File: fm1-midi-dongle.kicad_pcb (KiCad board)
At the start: 4 copper layers, 18.9 x 26 mm, 30 parts, among them J1 TYPE-C 24P-GTJB 040, J2 TYPE-C-31-M-12, J3 PJ-320D, J4 PJ-320D, U1 CH32X035G8U6, U2 XC6206P332MR, U3 SY6280AAC, U4 H11L1SM

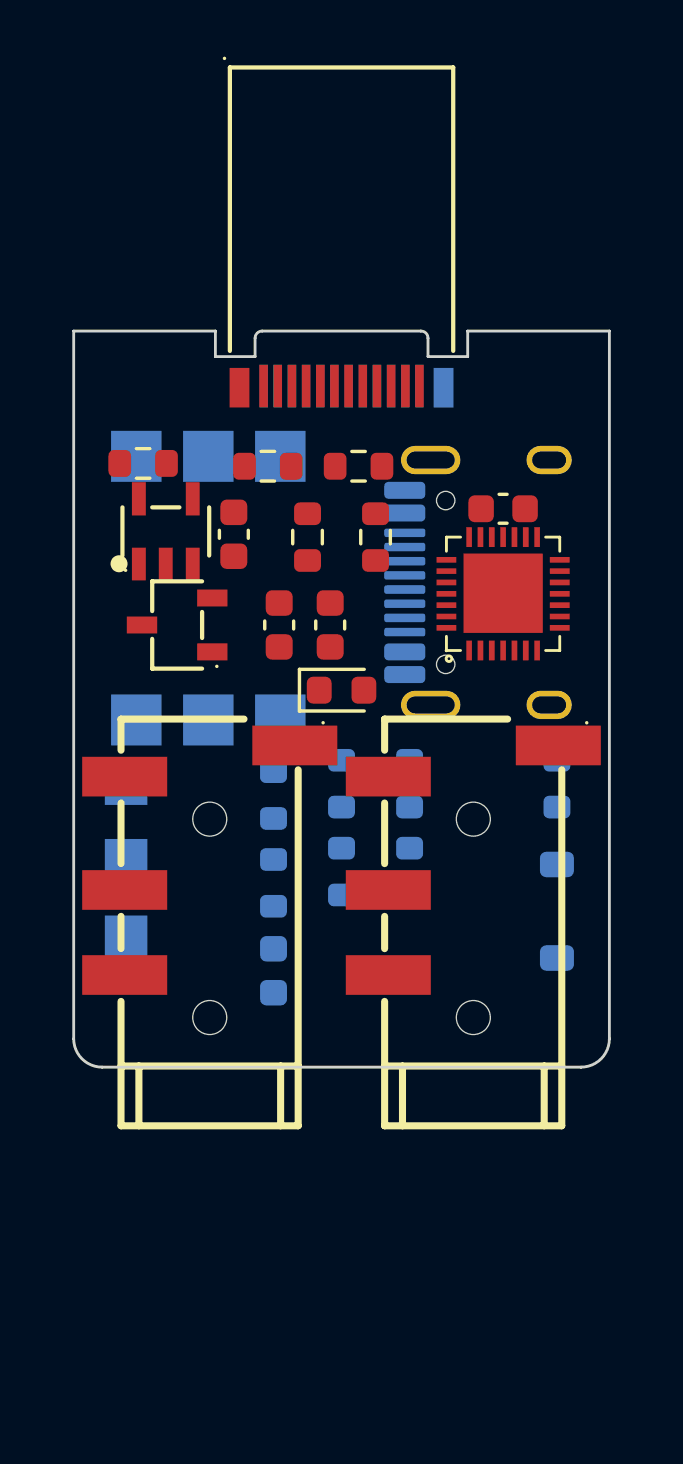
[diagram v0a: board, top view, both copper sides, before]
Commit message: Floorplan v2: signal-priority placement (USB pair straight under the plug, VBUS switch on the back-face pads, MIDI TX on top), 10 mm jack pitch, two inner GND planes, numeric pad-spacing and hole checks
Co-Authored-By: Claude Fable 5.1 <noreply@anthropic.com>
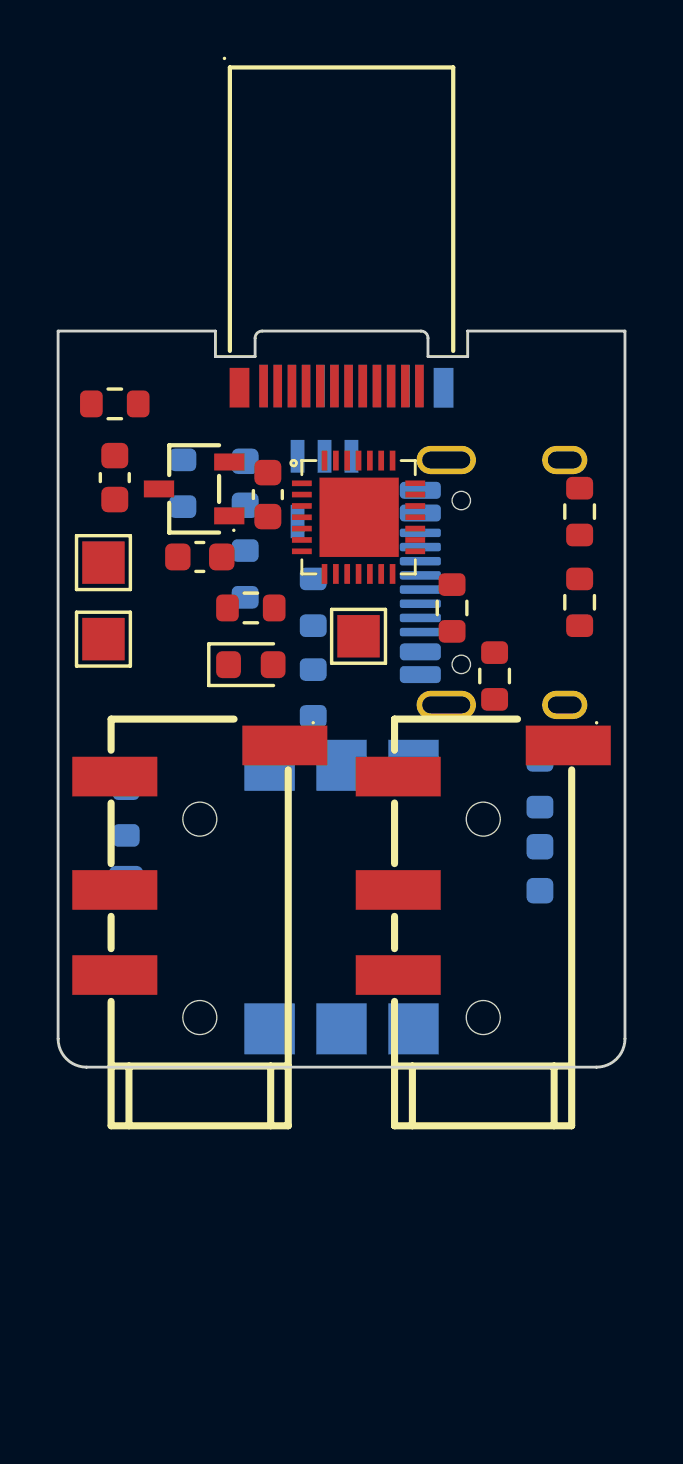
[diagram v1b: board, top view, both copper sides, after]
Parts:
- C3, R12, R4, U3: moved to B.Cu
- R11, R7, R8, TP1, TP2, TP3: moved to F.Cu
- moved D1 15.2 mm to (-7.60, 19.0)
- moved TP3 13.4 mm to (0.60, 8.80)
- moved R11 12.5 mm to (-3.20, 7.80), turned to 0 degrees
- moved U4 11.9 mm to (0.00, 18.0)
- moved R5 11.1 mm to (8.40, 4.40), turned to 90 degrees
- moved C5 10.1 mm to (7.00, 17.0)
- moved R10 10.0 mm to (7.00, 14.0)
- moved C1 9.21 mm to (-8.00, 3.20)
- moved R6 9.16 mm to (8.40, 7.60), turned to 90 degrees
- moved C4 8.32 mm to (-2.60, 3.80), turned to 90 degrees
- moved TP1 7.84 mm to (-8.40, 6.20)
- moved TP2 7.84 mm to (-8.40, 8.90)
- moved R8 7.52 mm to (5.40, 10.2)
- moved R12 7.06 mm to (-5.60, 3.40)
- moved R2 6.48 mm to (-1.00, 7.60)
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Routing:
- added copper zone on In2.Cu, net GND
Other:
- board size 18.9 x 26 mm -> 20 x 26 mm

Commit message: PCB v3: priority-driven floorplan and full routing, DRC 0 / unconnected 0
- USB pair straight under the plug on F.Cu over the GND plane, no vias; DNP pull-downs removed (internal ones used)
- VBUS on the plug's back-face pads only, SY6280 2.5 mm away on the back; In2 = +3V3 plane; vias tented
- 10 mm jack pitch, receptacle on the right side, clamp keep-out both faces, numeric pad/hole spacing checks
- routed with the KAT router (kicad-pcb-autorouter-workflow skill), cfg in tools/cfg_fm1.py; post-route GND via
- Gerbers, Excellon, JLCPCB CPL + BOM, 3D renders, HTML layer viewer

Co-Authored-By: Claude Fable 5.1 <noreply@anthropic.com>
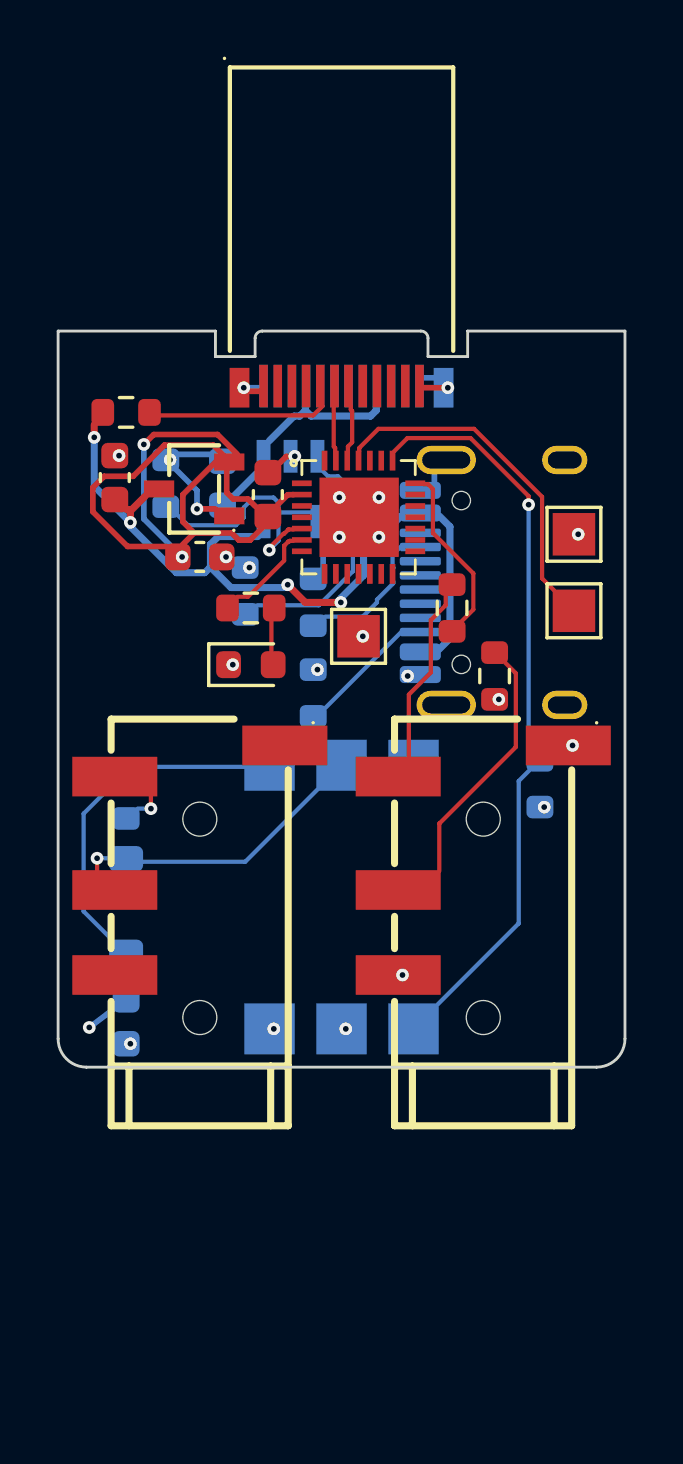
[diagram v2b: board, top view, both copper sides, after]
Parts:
- removed R5, R6: 15k, R_0603_1608Metric
- moved TP1 16.6 mm to (8.20, 5.20)
- moved TP2 16.6 mm to (8.20, 7.90)
- moved C5 15.6 mm to (-7.60, 22.4)
- moved U3 1.20 mm to (-1.80, 3.60)
- moved C3 0.80 mm to (-4.20, 3.40)
- moved D1 0.70 mm to (-7.60, 18.3)
- moved R12 0.60 mm to (-6.20, 3.40)
- moved R4 0.60 mm to (-3.40, 7.20)
- moved R9 0.60 mm to (-7.60, 14.4)
- moved R1 0.50 mm to (-7.60, 0.90)
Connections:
- J1 pad A4: /VBUS_FM1 -> (no net)
- J1 pad A9: /VBUS_FM1 -> (no net)
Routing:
- net +3V3: track 0.00 -> 28.2 mm, vias 0 -> 7
- net +5V_IN: track 0.00 -> 26.2 mm, vias 0 -> 4
- net /MIDI_RX: track 0.00 -> 24.4 mm, vias 0 -> 1
- net GND: track 0.00 -> 12.7 mm, vias 0 -> 20
- net /SDI_DIO: track 0.00 -> 11.3 mm
- net /OPTO_A: track 0.00 -> 10.3 mm
- net /MIDI_RING_OUT: track 0.00 -> 8.62 mm
- net /VBUS_EN: track 0.00 -> 8.56 mm, vias 0 -> 1
- net /MIDI_IN_RING: track 0.00 -> 8.18 mm, vias 0 -> 1
- net /ISET: track 0.00 -> 8.04 mm
- net /MIDI_TIP_OUT: track 0.00 -> 6.29 mm
- net /VBUS_FM1: track 0.00 -> 5.89 mm
- net /CC_FM1: track 0.00 -> 5.88 mm
- net /MIDI_TX: track 0.00 -> 5.80 mm
- net /CC1_IN: track 0.00 -> 4.40 mm
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- added copper zone on In2.Cu, net +3V3
- removed copper zone on In2.Cu, net GND

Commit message: Revert to placement only: routing was not asked for; board back to the v3 floorplan, fab outputs removed
Co-Authored-By: Claude Fable 5.1 <noreply@anthropic.com>
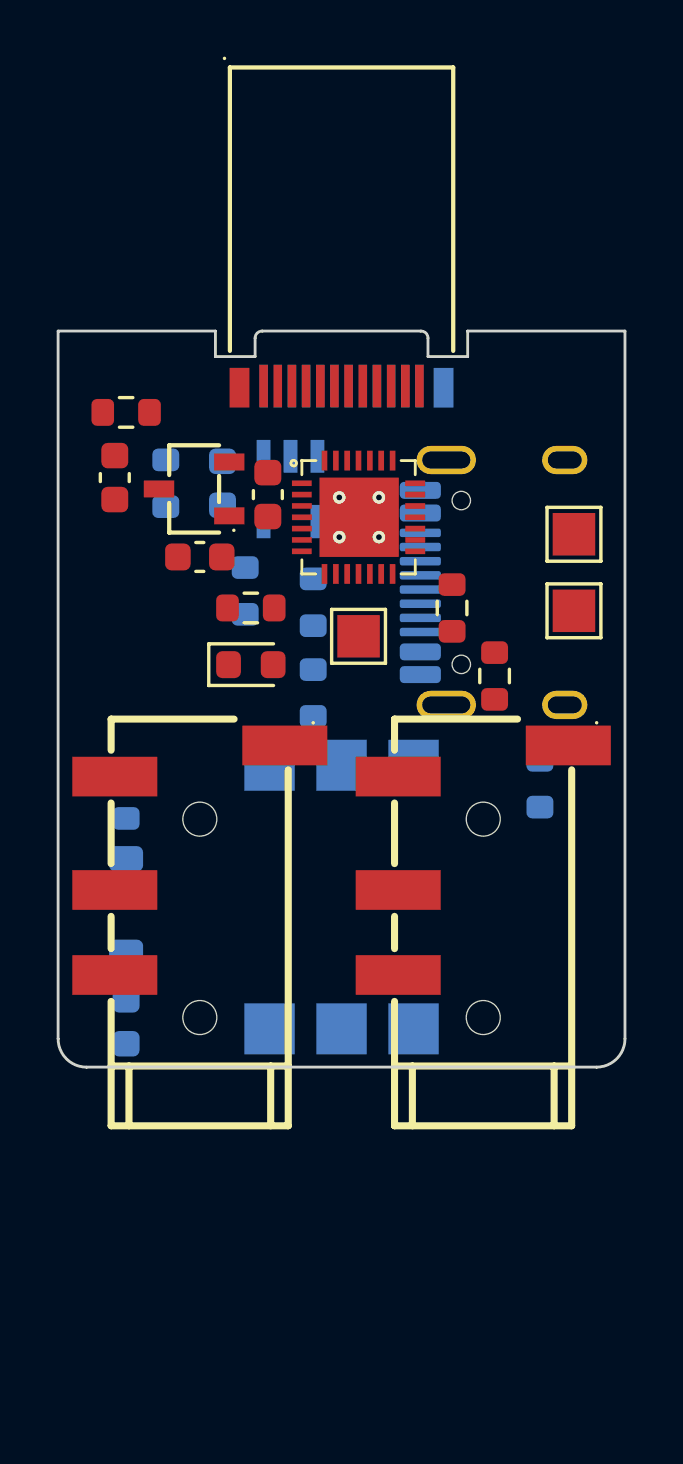
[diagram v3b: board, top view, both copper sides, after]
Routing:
- net +3V3: track 28.2 -> 0.00 mm, vias 7 -> 0
- net +5V_IN: track 26.2 -> 0.00 mm, vias 4 -> 0
- net /MIDI_RX: track 24.4 -> 0.00 mm, vias 1 -> 0
- net GND: track 12.7 -> 0.00 mm, vias 20 -> 4
- net /SDI_DIO: track 11.3 -> 0.00 mm
- net /OPTO_A: track 10.3 -> 0.00 mm
- net /MIDI_RING_OUT: track 8.62 -> 0.00 mm
- net /VBUS_EN: track 8.56 -> 0.00 mm, vias 1 -> 0
- net /MIDI_IN_RING: track 8.18 -> 0.00 mm, vias 1 -> 0
- net /ISET: track 8.04 -> 0.00 mm
- net /MIDI_TIP_OUT: track 6.29 -> 0.00 mm
- net /VBUS_FM1: track 5.89 -> 0.00 mm
- net /CC_FM1: track 5.88 -> 0.00 mm
- net /MIDI_TX: track 5.80 -> 0.00 mm
- net /CC1_IN: track 4.40 -> 0.00 mm
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
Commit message: PCB v4: single-sided placement, hand-written routing, silkscreen, rounded outline, case notches, 3D fixes
- gen_pcb.py: single-sided 20 x 37.7 mm floorplan, passives oriented toward their nets,
  convex corners rounded, two side locating notches (y 22.2, r 0.6) for a captured case,
  J2 3D offset fixed, KiCad-library models pointed at vendored STEP files
- route.py: explicit polylines (no autorouter), 45 deg bends only, no loops,
  0.2/0.3/0.5 mm tracks, 0.6/0.3 and 0.8/0.4 vias, GND planes and pours, +5V_IN pour
- silk.py: regenerated silkscreen (clipped outlines, pin-1/cathode marks, 0.8 mm
  designators, test-pad and back labels)
- check_loops.py, render_nets.py, render_route.py: review tools and renders in docs/
- house_rules.yaml + .kicad_dru: project rule override (USB plain 0.2 mm)
- plug WRL made opaque; R/C/LED 0603 and SOD-123 STEP vendored (KiCad 3D lib, CC-BY-SA 4.0)
- schematic: plug A9 NC (VBUS on A4/B4/B9)

DRC: 0 unconnected, 0 clearance errors; accepted items listed in DESIGN.md.

Co-Authored-By: Claude Opus 5.5 <noreply@anthropic.com>
Claude-Session: https://claude.ai/code/session_01Dtfv3zuhZTs975LiSXznFQ
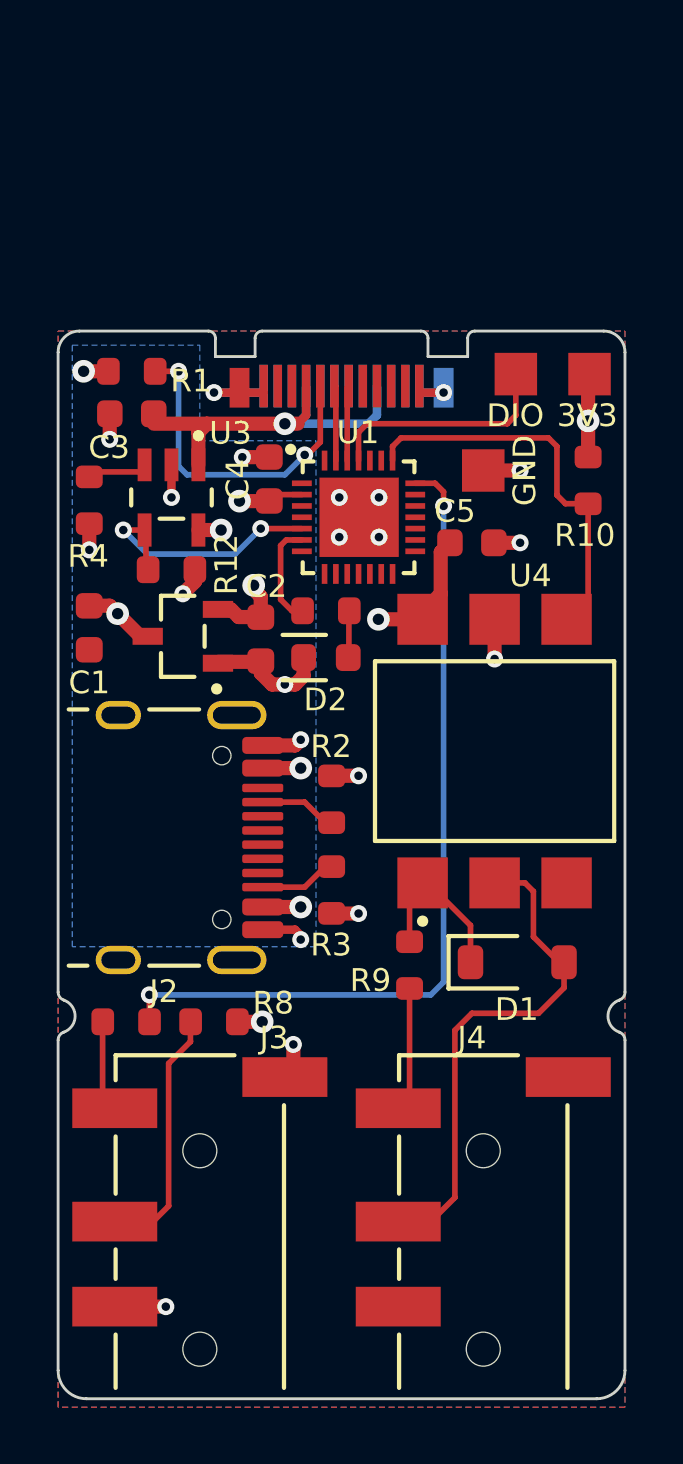
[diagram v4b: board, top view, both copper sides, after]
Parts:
- C3, C5, D1, J2, R10, R12, R2, R3, R4, R9, U3, U4: moved to F.Cu
- moved C5 20.8 mm to (4.60, 5.50), turned to 0 degrees
- moved R7 18.6 mm to (-7.60, 22.4), turned to 180 degrees
- moved J2 16.4 mm to (-6.83, 15.9)
- moved R8 15.7 mm to (-4.50, 22.4), turned to 180 degrees
- moved J3 15.4 mm to (-5.00, 28.4)
- moved J4 15.4 mm to (5.00, 28.4)
- moved D1 13.9 mm to (6.20, 20.3), turned to 0 degrees
- moved R9 11.7 mm to (2.40, 20.4)
- moved R10 10.8 mm to (8.70, 3.30), turned to -90 degrees
- moved TP2 8.60 mm to (6.15, -0.45)
- moved U4 7.46 mm to (5.40, 12.8)
- moved TP3 7.32 mm to (5.00, 2.95)
- moved R2 6.98 mm to (-0.35, 14.6)
- moved R3 6.98 mm to (-0.35, 17.8), turned to -90 degrees
- moved R4 6.36 mm to (-8.90, 4.00), turned to -90 degrees
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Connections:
- J1 pad A4: (no net) -> /VBUS_FM1
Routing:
- net /MIDI_TX: track 0.00 -> 29.9 mm, vias 0 -> 2
- net GND: track 0.00 -> 26.1 mm, vias 4 -> 21
- net /MIDI_IN_RING: track 0.00 -> 18.2 mm
- net /VBUS_FM1: track 0.00 -> 13.9 mm, vias 0 -> 1
- net +3V3: track 0.00 -> 13.1 mm, vias 0 -> 5
- net /MIDI_RX: track 0.00 -> 13.0 mm
- net /CC_FM1: track 0.00 -> 11.7 mm, vias 0 -> 2
- net /MIDI_RING_OUT: track 0.00 -> 8.95 mm
- net /VBUS_EN: track 0.00 -> 8.77 mm, vias 0 -> 2
- net /SDI_DIO: track 0.00 -> 8.25 mm
- net +5V_IN: track 0.00 -> 6.87 mm, vias 0 -> 5
- net /OPTO_A: track 0.00 -> 4.28 mm
- net /MIDI_IN_TIP: track 0.00 -> 4.22 mm
- net /LED: track 0.00 -> 3.67 mm
- net /MIDI_TIP_OUT: track 0.00 -> 3.05 mm
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- added copper zone on B.Cu, net +5V_IN
- added copper zone on B.Cu, net GND
- added copper zone on F.Cu, net GND
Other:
- board size 20 x 26 mm -> 20 x 37.7 mm
- board text added: "3V3"
- board text added: "5V IN"
- board text added: "DIO"
- board text added: "FM-1 MIDI"
- board text added: "GND"
- board text added: "MIDI IN"
- board text added: "MIDI OUT"
- board text added: "TRS type A"
- board text added: "dongle"
- board text added: "v4 2026-10"

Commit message: D2 to Basic red LED C2286 (green C72043 out of stock); add 3D views
- gen_sch.py / BOM.csv: D2 KT-0603R (C2286, Basic): no Extended fee, ~1.3 mA via R11 1k
- schematic and board regenerated: ERC 0, DRC unchanged (accepted items only)
- docs/views: top, bottom, isometric front/back/under, side and front renders

Co-Authored-By: Claude Opus 5.5 <noreply@anthropic.com>
Claude-Session: https://claude.ai/code/session_01Dtfv3zuhZTs975LiSXznFQ
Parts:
- D2: value LED green 0603 -> LED red 0603
